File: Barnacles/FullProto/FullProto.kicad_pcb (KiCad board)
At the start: 2 copper layers, 82.5 x 48.3 mm, 16 parts, among them J1 Conn_01x01, J12 Conn_02x03_Top_Bottom, J13 Conn_02x03_Top_Bottom, J2 Conn_01x01, J3 Conn_01x01, J4 Conn_01x01, J5 Conn_01x01, J6 Conn_01x01

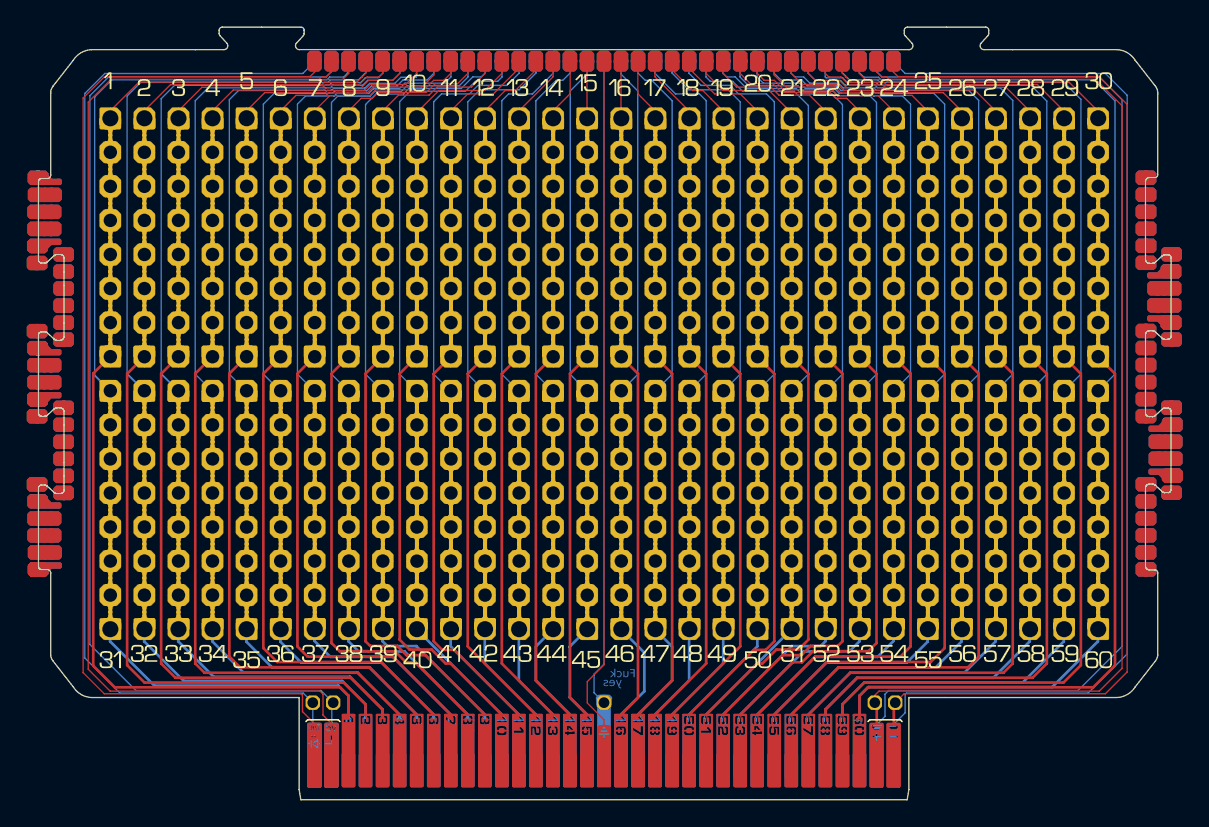
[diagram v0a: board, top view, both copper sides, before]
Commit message: add wigs
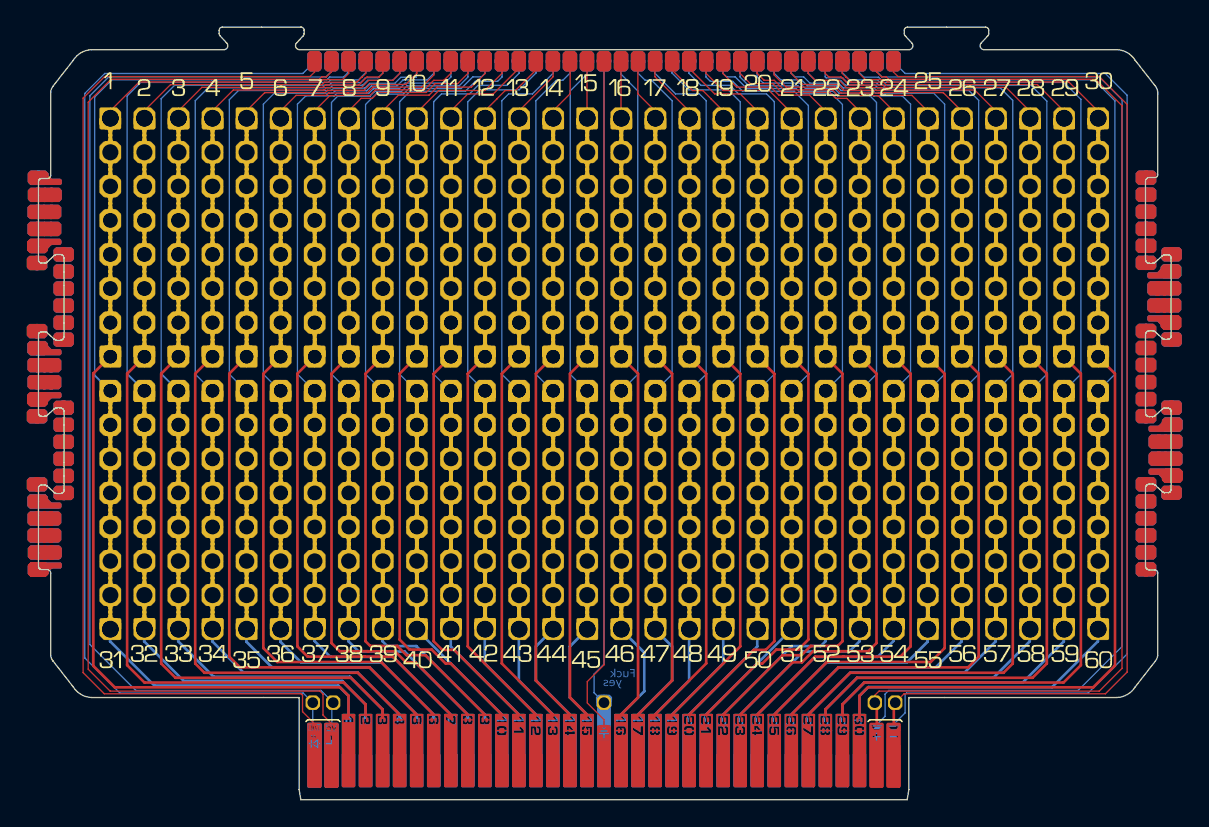
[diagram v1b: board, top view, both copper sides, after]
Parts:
- added REF** (x2): Conn_8x30_drillPlated, JumperlessFootprints:Conn_8x30_drillPlated, F.Cu at (155.2, 44.6)
